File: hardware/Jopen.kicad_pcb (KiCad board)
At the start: 2 copper layers, 113 x 71.9 mm, 150 parts, among them J6 Screw_Terminal_01x18, J7 Screw_Terminal_01x18, U1 STM32F102RBTx, U2 TPS7B6933QDCYRQ1, U3 SN65HVD1786D, Y1 8 MHz

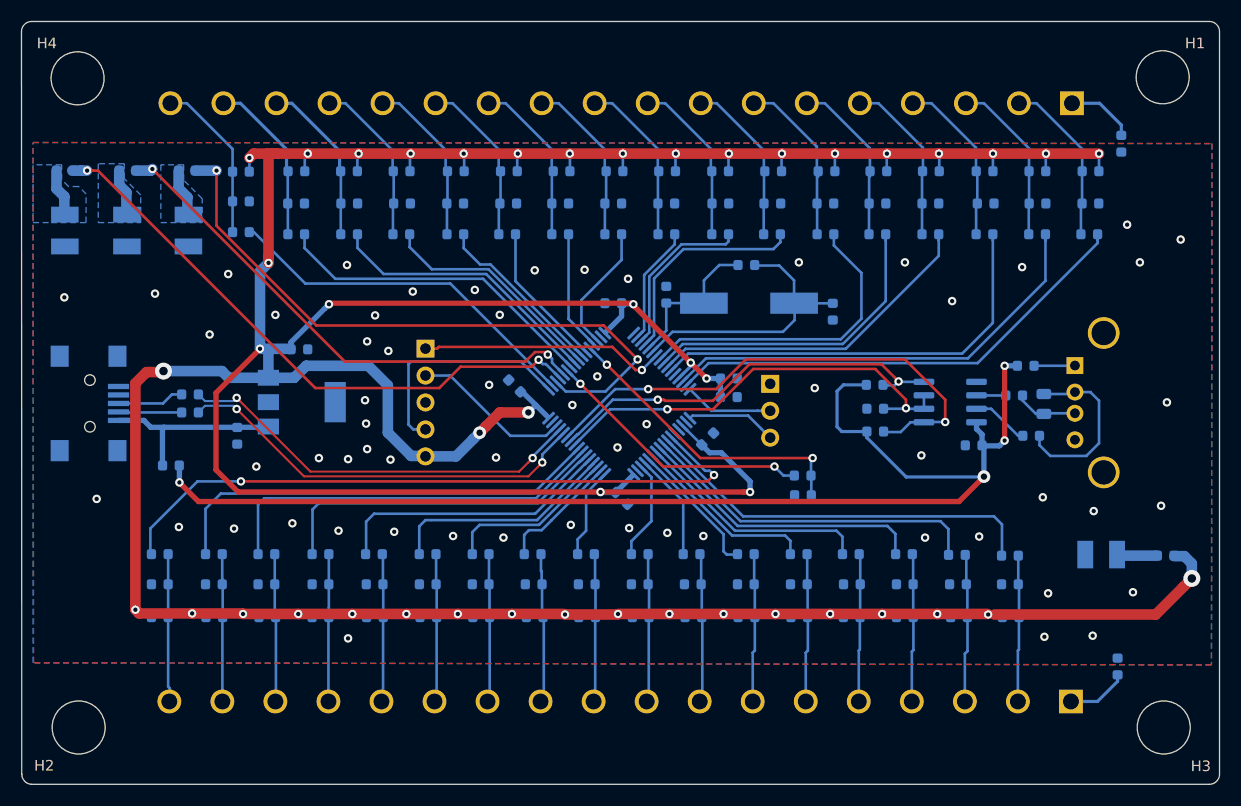
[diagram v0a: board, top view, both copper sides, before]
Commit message: Fix P1 IN3 and P2 ADC4 pin configuration
Firmware changes:
- Disabled ADC peripheral initialization (MX_ADC1_Init and HAL_ADC_MspInit)
- Added GPIO pull-up resistors for all button inputs (active-low logic)
- Fixed keyboard HID descriptor (6KRO standard format, 47 bytes)
- Added LED debug indicators (LED1=P1, LED2=P2)
- Device name now conditional based on mode (Keyboard/Joystick/JVS)
- Fixed pin mappings for dual arcade controls (34 inputs total)

Hardware changes:
- Updated KiCad files (v6+ format)
- Added netlist (Jopen.net) for pin verification
- Added flash.ps1 script for automated programming
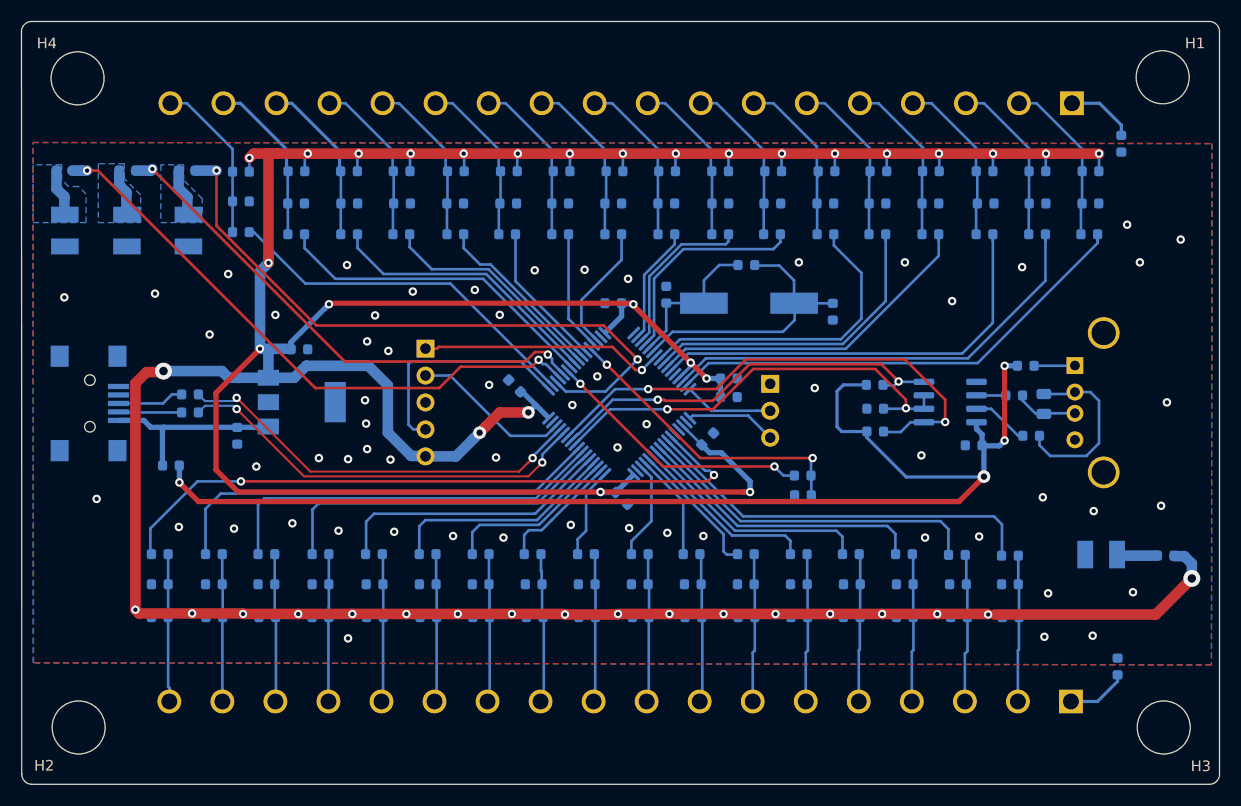
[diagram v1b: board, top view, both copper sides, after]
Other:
- outline, holes or cut-outs redrawn
- net class Default removed
